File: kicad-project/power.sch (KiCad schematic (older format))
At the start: 8 parts

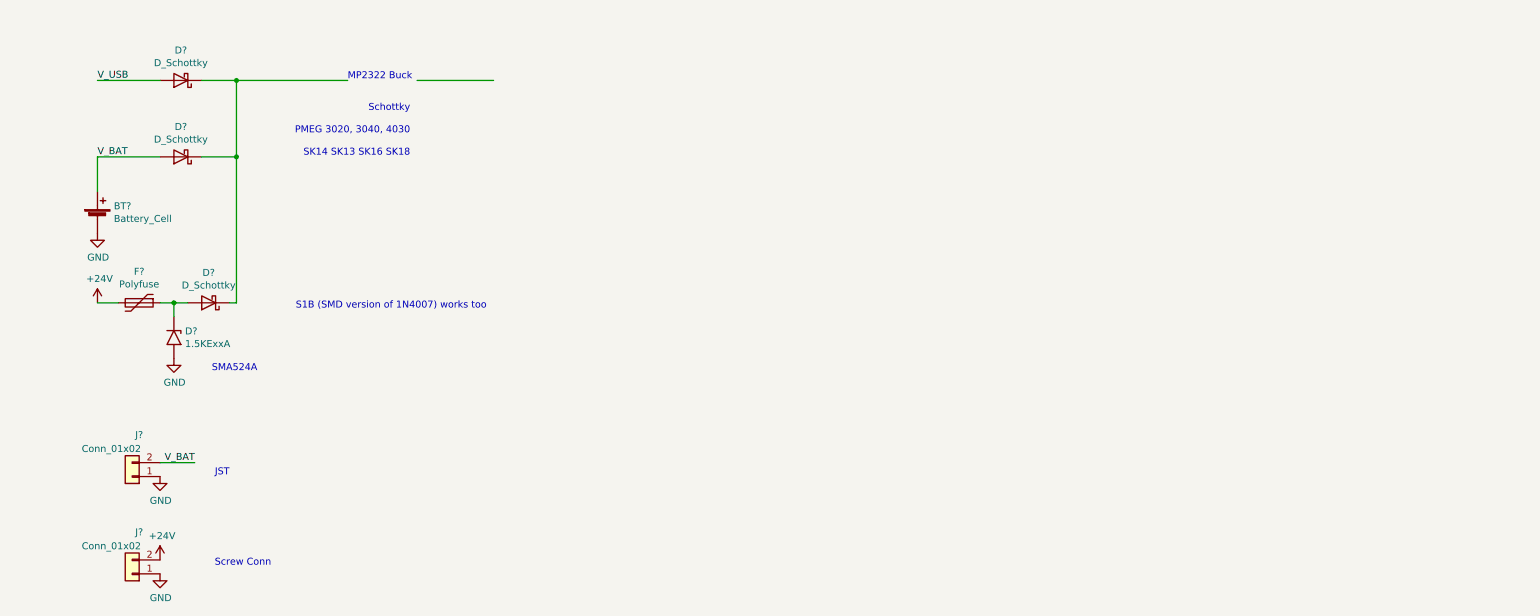
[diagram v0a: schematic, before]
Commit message: sch: add gps
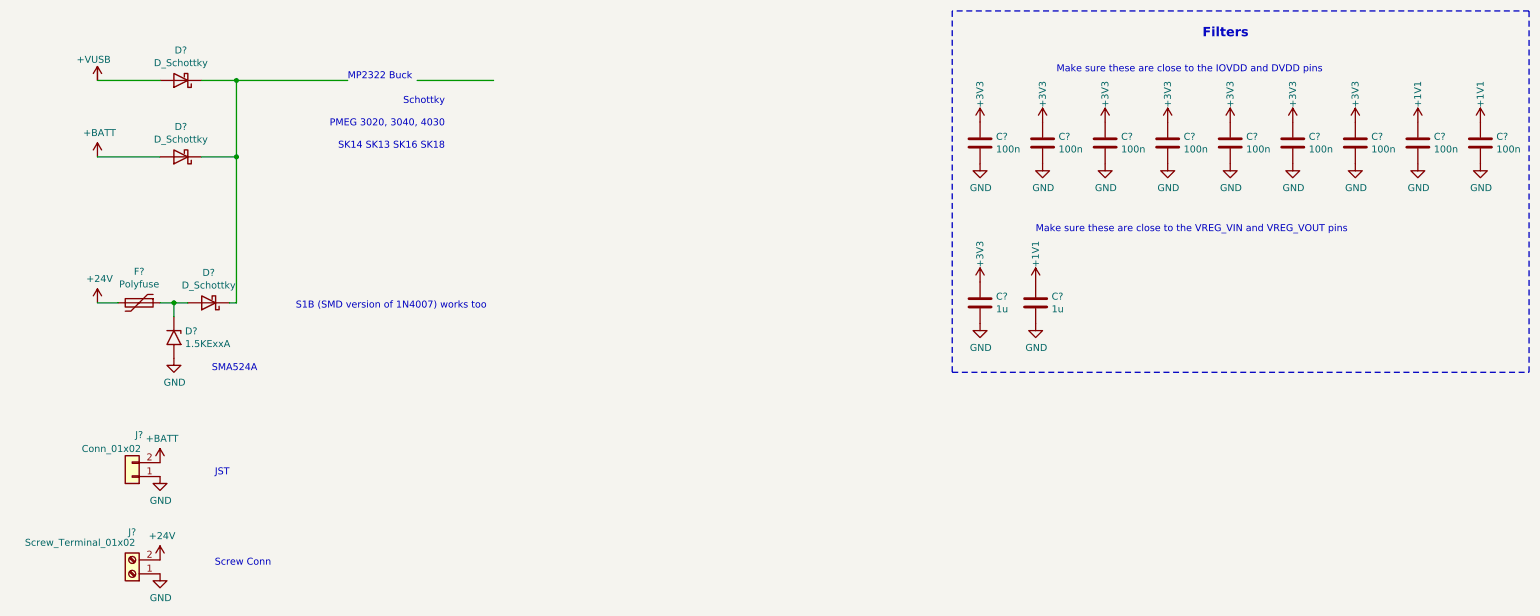
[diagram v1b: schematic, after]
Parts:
- removed BT?: Battery_Cell, symbol Device:Battery_Cell
- removed J?: Conn_01x02, symbol Connector_Generic:Conn_01x02
- added C? (x9): 100n, Capacitor_SMD:C_0603_1608Metric, symbol Device:C
- added C? (x2): 1u, Capacitor_SMD:C_0603_1608Metric, symbol Device:C
- added J?: Screw_Terminal_01x02, symbol Connector:Screw_Terminal_01x02
- added V?: +VUSB, symbol AA_PPSE_2021:+VUSB
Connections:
- net labels added: +1V1, +3V3, +BATT
- net labels removed: V_BAT, V_USB
- wire segments 15 -> 13
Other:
- note added: "Filters"
- note added: "Make sure these are close to the IOVDD and DVDD pins"
- note added: "Make sure these are close to the VREG_VIN and VREG_VOUT pins"
